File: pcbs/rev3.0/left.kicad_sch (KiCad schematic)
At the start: 30 parts, among them J1 Conn_ST_STDC14, SW65 MK-12C03-G015, U1 LDI1117, U2 USBLC6-2SC6_C5261088, U3 358, U4 STM32F446RCTx, U5 GT-TC020A-H035-L05, Y1 8MHz

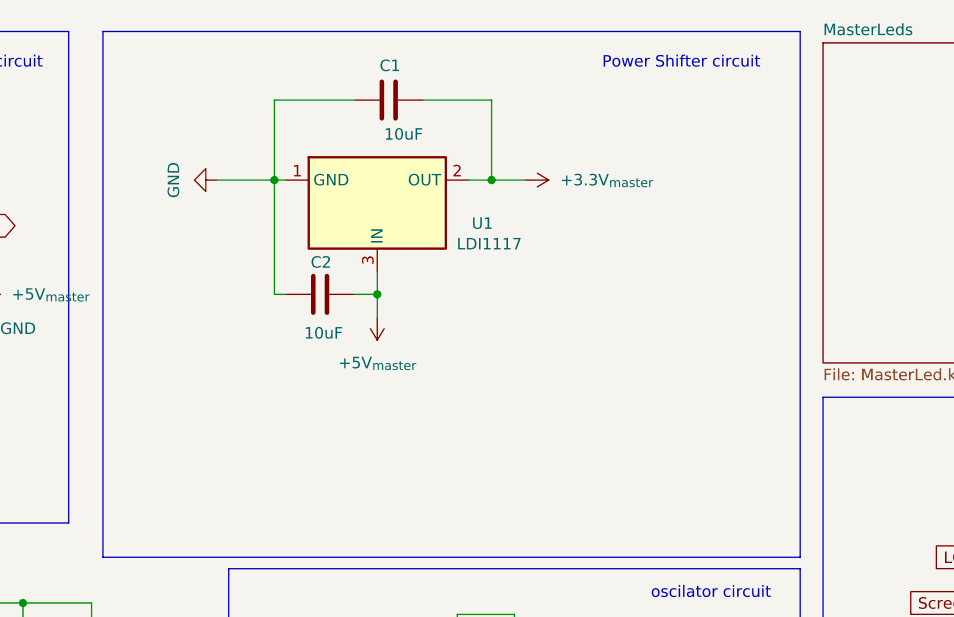
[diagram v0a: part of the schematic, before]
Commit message: Change LDI3.3 LCSC part number to Diotec part
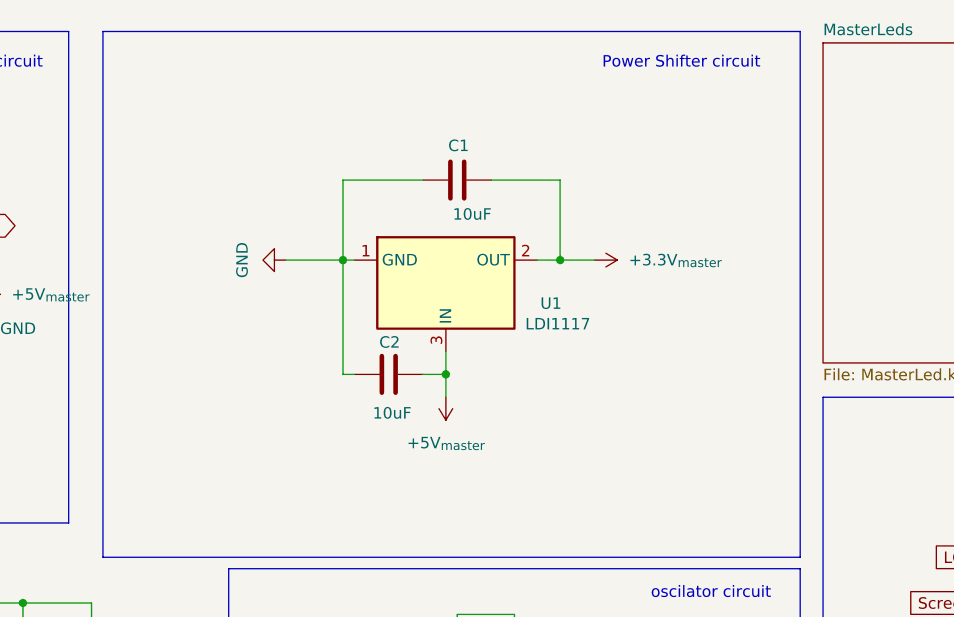
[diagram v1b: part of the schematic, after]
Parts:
- U1: LCSC C6186 -> (none); LCSC Part C6186 -> (none)
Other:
- moved on the sheet: C1, C2, U1
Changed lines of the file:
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@@
 	)
 	(junction
-		(at 167.64 30.48)
+		(at 175.26 39.37)
 		(diameter 0)
 		(color 0 0 0 0)
@@
 	)
 	(junction
-		(at 154.94 43.18)
+		(at 162.56 52.07)
 		(diameter 0)
 		(color 0 0 0 0)
@@
 	)
 	(junction
-		(at 143.51 30.48)
+		(at 151.13 39.37)
 		(diameter 0)
 		(color 0 0 0 0)
@@
 	(wire
 		(pts
-			(xy 167.64 30.48) (xy 171.45 30.48)
+			(xy 175.26 39.37) (xy 179.07 39.37)
 		)
 		(stroke
@@
 	(wire
 		(pts
-			(xy 143.51 21.59) (xy 143.51 30.48)
+			(xy 151.13 30.48) (xy 151.13 39.37)
 		)
 		(stroke
@@
 	(wire
 		(pts
-			(xy 167.64 30.48) (xy 167.64 21.59)
+			(xy 175.26 39.37) (xy 175.26 30.48)
 		)
 		(stroke
@@
 	(wire
 		(pts
-			(xy 152.4 43.18) (xy 154.94 43.18)
+			(xy 160.02 52.07) (xy 162.56 52.07)
 		)
 		(stroke
@@
 	(wire
 		(pts
-			(xy 137.16 30.48) (xy 143.51 30.48)
+			(xy 144.78 39.37) (xy 151.13 39.37)
 		)
 		(stroke
@@
 	(wire
 		(pts
-			(xy 154.94 45.72) (xy 154.94 43.18)
+			(xy 162.56 54.61) (xy 162.56 52.07)
 		)
 		(stroke
@@
 	(wire
 		(pts
-			(xy 143.51 43.18) (xy 144.78 43.18)
+			(xy 151.13 52.07) (xy 152.4 52.07)
 		)
 		(stroke
@@
 	(wire
 		(pts
-			(xy 143.51 30.48) (xy 143.51 43.18)
+			(xy 151.13 39.37) (xy 151.13 52.07)
 		)
 		(stroke
@@
 	(wire
 		(pts
-			(xy 152.4 21.59) (xy 143.51 21.59)
+			(xy 160.02 30.48) (xy 151.13 30.48)
 		)
 		(stroke
@@
 	(wire
 		(pts
-			(xy 167.64 21.59) (xy 160.02 21.59)
+			(xy 175.26 30.48) (xy 167.64 30.48)
 		)
 		(stroke
@@
 	(wire
 		(pts
-			(xy 165.1 30.48) (xy 167.64 30.48)
+			(xy 172.72 39.37) (xy 175.26 39.37)
 		)
 		(stroke
@@
 	(wire
 		(pts
-			(xy 154.94 43.18) (xy 154.94 40.64)
+			(xy 162.56 52.07) (xy 162.56 49.53)
 		)
 		(stroke
@@
 	(wire
 		(pts
-			(xy 143.51 30.48) (xy 144.78 30.48)
+			(xy 151.13 39.37) (xy 152.4 39.37)
 		)
 		(stroke
@@
 	(symbol
 		(lib_id "power:+3.3V")
-		(at 171.45 30.48 270)
+		(at 179.07 39.37 270)
 		(unit 1)
 		(exclude_from_sim no)
@@
 		(fields_autoplaced yes)
 		(property "Reference" "#PWR03"
-			(at 167.64 30.48 0)
+			(at 175.26 39.37 0)
 			(effects
 				(font
@@
 		)
 		(property "Value" "+3.3V_{master}"
-			(at 175.26 30.4799 90)
+			(at 182.88 39.3699 90)
 			(effects
 				(font
@@
 		)
 		(property "Footprint" ""
-			(at 171.45 30.48 0)
+			(at 179.07 39.37 0)
 			(effects
 				(font
@@
 		)
 		(property "Datasheet" ""
-			(at 171.45 30.48 0)
+			(at 179.07 39.37 0)
 			(effects
 				(font
@@
 		)
 		(property "Description" "Power symbol creates a global label with name \"+3.3V\""
-			(at 171.45 30.48 0)
+			(at 179.07 39.37 0)
 			(effects
 				(font
@@
 	(symbol
 		(lib_id "Device:C")
-		(at 156.21 21.59 270)
+		(at 163.83 30.48 270)
 		(unit 1)
 		(exclude_from_sim no)
@@
 		(dnp no)
 		(property "Reference" "C1"
-			(at 155.194 17.78 90)
+			(at 162.814 26.67 90)
 			(effects
 				(font
@@
 		)
 		(property "Value" "10uF"
-			(at 155.702 25.4 90)
+			(at 163.322 34.29 90)
 			(effects
 				(font
@@
 		)
 		(property "Footprint" "Capacitor_SMD:C_1206_3216Metric"
-			(at 152.4 22.5552 0)
+			(at 160.02 31.4452 0)
 			(effects
 				(font
@@
 		)
 		(property "Datasheet" "~"
-			(at 156.21 21.59 0)
+			(at 163.83 30.48 0)
 			(effects
 				(font
@@
 		)
 		(property "Description" "Unpolarized capacitor"
-			(at 156.21 21.59 0)
+			(at 163.83 30.48 0)
 			(effects
 				(font
@@
 		)
 		(property "LCSC" "C13585"
-			(at 156.21 21.59 0)
+			(at 163.83 30.48 0)
 			(effects
 				(font
@@
 		)
 		(property "LCSC Part" "C13585"
-			(at 156.21 21.59 0)
+			(at 163.83 30.48 0)
 			(effects
 				(font
@@
 	(symbol
 		(lib_id "power:+5V")
-		(at 154.94 45.72 180)
+		(at 162.56 54.61 180)
 		(unit 1)
 		(exclude_from_sim no)
@@
 		(fields_autoplaced yes)
 		(property "Reference" "#PWR09"
-			(at 154.94 41.91 0)
+			(at 162.56 50.8 0)
 			(effects
 				(font
@@
 		)
 		(property "Value" "+5V_{master}"
-			(at 154.94 50.8 0)
+			(at 162.56 59.69 0)
 			(effects
 				(font
@@
 		)
 		(property "Footprint" ""
-			(at 154.94 45.72 0)
+			(at 162.56 54.61 0)
 			(effects
 				(font
@@
 		)
 		(property "Datasheet" ""
-			(at 154.94 45.72 0)
+			(at 162.56 54.61 0)
 			(effects
 				(font
@@
 		)
 		(property "Description" "Power symbol creates a global label with name \"+5V\""
-			(at 154.94 45.72 0)
+			(at 162.56 54.61 0)
 			(effects
 				(font
@@
 	(symbol
 		(lib_id "Device:C")
-		(at 148.59 43.18 90)
+		(at 156.21 52.07 90)
 		(unit 1)
 		(exclude_from_sim no)
@@
 		(dnp no)
 		(property "Reference" "C2"
-			(at 149.86 39.624 90)
+			(at 157.48 48.514 90)
 			(effects
 				(font
@@
 		)
 		(property "Value" "10uF"
-			(at 151.13 47.498 90)
+			(at 158.75 56.388 90)
 			(effects
 				(font
@@
 		)
 		(property "Footprint" "Capacitor_SMD:C_1206_3216Metric"
-			(at 152.4 42.2148 0)
+			(at 160.02 51.1048 0)
 			(effects
 				(font
@@
 		)
 		(property "Datasheet" "~"
-			(at 148.59 43.18 0)
+			(at 156.21 52.07 0)
 			(effects
 				(font
@@
 		)
 		(property "Description" "Unpolarized capacitor"
-			(at 148.59 43.18 0)
+			(at 156.21 52.07 0)
 			(effects
 				(font
@@
 		)
 		(property "LCSC" "C13585"
-			(at 148.59 43.18 0)
+			(at 156.21 52.07 0)
 			(effects
 				(font
@@
 		)
 		(property "LCSC Part" "C13585"
-			(at 148.59 43.18 0)
+			(at 156.21 52.07 0)
 			(effects
 				(font
@@
 	(symbol
 		(lib_id "power:GND")
-		(at 137.16 30.48 270)
+		(at 144.78 39.37 270)
 		(unit 1)
 		(exclude_from_sim no)
@@
 		(dnp no)
 		(property "Reference" "#PWR02"
-			(at 130.81 30.48 0)
+			(at 138.43 39.37 0)
 			(effects
 				(font
@@
 		)
 		(property "Value" "GND"
-			(at 132.334 30.48 0)
+			(at 139.954 39.37 0)
 			(effects
 				(font
@@
 		)
 		(property "Footprint" ""
-			(at 137.16 30.48 0)
+			(at 144.78 39.37 0)
 			(effects
 				(font
@@
 		)
 		(property "Datasheet" ""
-			(at 137.16 30.48 0)
+			(at 144.78 39.37 0)
 			(effects
 				(font
@@
 		)
 		(property "Description" "Power symbol creates a global label with name \"GND\" , ground"
-			(at 137.16 30.48 0)
+			(at 144.78 39.37 0)
 			(effects
 				(font
@@
 	(symbol
 		(lib_id "Regulator_Linear:LT1963AxST-3.3")
-		(at 154.94 33.02 0)
+		(at 162.56 41.91 0)
 		(unit 1)
 		(exclude_from_sim no)
@@
 		(dnp no)
 		(property "Reference" "U1"
-			(at 166.624 35.306 0)
+			(at 174.244 44.196 0)
 			(effects
 				(font
@@
 		)
 		(property "Value" "LDI1117"
-			(at 167.386 37.592 0)
+			(at 175.006 46.482 0)
 			(effects
 				(font
@@
 		)
 		(property "Footprint" "Package_TO_SOT_SMD:SOT-223-3_TabPin2"
-			(at 154.94 44.45 0)
+			(at 162.56 53.34 0)
 			(effects
 				(font
@@
 			)
 		)
-		(property "Datasheet" "https://www.lcsc.com/datasheet/C6186.pdf"
-			(at 154.94 46.99 0)
+		(property "Datasheet" ""
+			(at 162.56 55.88 0)
 			(effects
 				(font
@@
 			)
 		)
-		(property "Description" "Advanced Monolithic Systems AMS1117-3.3"
-			(at 154.94 33.02 0)
+		(property "Description" ""
+			(at 162.56 41.91 0)
 			(effects
 				(font
@@
 			)
 		)
-		(property "LCSC" "C6186"
-			(at 154.94 33.02 0)
+		(property "LCSC" ""
+			(at 162.56 41.91 0)
 			(effects
 				(font
@@
 			)
 		)
-		(property "LCSC Part" "C6186"
-			(at 154.94 33.02 0)
+		(property "LCSC Part" ""
+			(at 162.56 41.91 0)
 			(effects
 				(font
